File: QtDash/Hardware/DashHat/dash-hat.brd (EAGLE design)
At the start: 107.8 x 66.8 mm, 163 parts, among them IC1 LMV614, IC2 MCP3X083008, IC3 MCP23017SS, IC4 LM358D, IC5 IL300, IC6 TSV912D, IC7 IL300, IC8 TSV912D, IC9 DS1374, J1 CONN_20X2, J10 455-1750-1-ND, J11 455-1750-1-ND, J15 VSS_IN, J16 TACH_IN, J6 VOLVO_CONN_31, J7 VOLVO_CONN_32, J8 455-1750-1-ND, J9 455-1750-1-ND, Y1 ECX-.327-6-34RR

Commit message: bugfix/hardware-revA-issues: 	- moved alternator D+ supply to fuse 16 12V supply 	- added datasheet for new LED backlit screen 	- added mount stls
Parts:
- moved R82 42.7 mm to (105.2, 21.3), turned to 270 degrees
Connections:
- net 12V: no longer R82.2
- net 12V-FUSE_16: now also R82.2
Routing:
- net CHARGING_N: track 44.6 -> 30.9 mm
- net 12V-FUSE_16: track 0.00 -> 12.4 mm
- net OUT9: track 26.8 -> 29.1 mm
- net OUT10: track 24.7 -> 26.3 mm
- net GND: vias 36 -> 38
- added copper zone on layer 1, net 12V-FUSE_16
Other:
- board size 107.8 x 66.8 mm -> 110.9 x 66.8 mm
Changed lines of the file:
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@@
 <setting verticaltext="up"/>
 </settings>
-<grid distance="10" unitdist="mil" unit="mil" style="lines" multiple="1" display="yes" altdistance="1" altunitdist="mil" altunit="mil"/>
+<grid distance="5" unitdist="mil" unit="mil" style="lines" multiple="1" display="yes" altdistance="1" altunitdist="mil" altunit="mil"/>
 <layers>
 <layer number="1" name="Top" color="4" fill="1" visible="yes" active="yes"/>
@@
 <hole x="4.142" y="3.5" drill="2.75"/>
 <hole x="4.142" y="61.5" drill="2.75"/>
-<wire x1="107.95" y1="63.792" x2="107.95" y2="2.746" width="0.4064" layer="20"/>
-<wire x1="107.95" y1="2.746" x2="104.95" y2="0" width="0.4064" layer="20" curve="-90"/>
-<wire x1="104.95" y1="0" x2="3.142" y2="0" width="0.4064" layer="20"/>
+<wire x1="110.998" y1="63.792" x2="110.998" y2="2.746" width="0.4064" layer="20"/>
+<wire x1="110.998" y1="2.746" x2="107.998" y2="0" width="0.4064" layer="20" curve="-90"/>
+<wire x1="107.998" y1="0" x2="3.142" y2="0" width="0.4064" layer="20"/>
 <wire x1="3.142" y1="0" x2="0.142" y2="3" width="0.4064" layer="20" curve="-90"/>
 <wire x1="0.142" y1="3" x2="0.142" y2="65.062" width="0.4064" layer="20"/>
@@
 <wire x1="57.15" y1="64.516" x2="57.15" y2="66.08343125" width="0.4064" layer="20"/>
 <wire x1="57.15" y1="66.08343125" x2="57.86856875" y2="66.80185" width="0.4064" layer="20" curve="-90.011963"/>
-<wire x1="57.86856875" y1="66.80185" x2="104.696" y2="66.792" width="0.4064" layer="20"/>
-<wire x1="104.696" y1="66.792" x2="107.95" y2="63.792" width="0.4064" layer="20" curve="-90"/>
+<wire x1="57.86856875" y1="66.80185" x2="107.744" y2="66.792" width="0.4064" layer="20"/>
+<wire x1="107.744" y1="66.792" x2="110.998" y2="63.792" width="0.4064" layer="20" curve="-90"/>
 <text x="50.038" y="63.754" size="1.016" layer="25" font="vector" rot="R180">Volvo 240 Pi Dash Adapter
 Rev B. Jan 2022
@@
 <wire x1="7.8618" y1="25.233" x2="9.8618" y2="25.233" width="0.001" layer="57"/>
 <wire x1="7.8618" y1="21.433" x2="7.8618" y2="25.233" width="0.001" layer="57"/>
+<hole x="107.752" y="3.5" drill="2.75"/>
+<hole x="107.752" y="61.5" drill="2.75"/>
 </plain>
 <attributes>
@@
 <element name="R78" library="digital_dash" package="0603" value="1k" x="9.652" y="59.69" rot="R180"/>
 <element name="R79" library="digital_dash" package="0603" value="1k" x="14.732" y="59.69" rot="R180"/>
-<element name="R82" library="resistor" package="0617/17" value="" x="95.758" y="62.992" rot="R180"/>
+<element name="R82" library="resistor" package="0617/17" value="" x="105.156" y="21.336" rot="R270"/>
 </elements>
 <signals>
@@
 <wire x1="27.94" y1="53.086" x2="27.94" y2="53.848" width="0.3048" layer="1"/>
 <wire x1="27.92" y1="53.086" x2="27.94" y2="53.086" width="0.3048" layer="1"/>
+<via x="33.909" y="33.274" extent="1-16" drill="0.5"/>
+<via x="33.909" y="32.258" extent="1-16" drill="0.5"/>
 </signal>
 <signal name="5V">
@@
 <wire x1="80.838" y1="23.03" x2="80.754" y2="23.114" width="0.6096" layer="16"/>
 <wire x1="80.754" y1="23.114" x2="79.375" y2="23.114" width="0.6096" layer="16"/>
-<contactref element="R82" pad="2"/>
 <via x="77.47" y="63.754" extent="1-16" drill="0.5"/>
 <via x="80.01" y="65.024" extent="1-16" drill="0.5"/>
@@
 <wire x1="41.891" y1="31.935" x2="41.91" y2="31.916" width="0.3048" layer="1"/>
 <wire x1="41.91" y1="31.916" x2="41.91" y2="26.67" width="0.3048" layer="1"/>
-<wire x1="41.91" y1="26.67" x2="49.872" y2="18.708" width="0.3048" layer="1"/>
-<wire x1="49.872" y1="18.708" x2="55.118" y2="18.708" width="0.3048" layer="1"/>
 <wire x1="57.9755" y1="18.542" x2="57.8095" y2="18.708" width="0.3048" layer="1"/>
 <wire x1="57.8095" y1="18.708" x2="55.118" y2="18.708" width="0.3048" layer="1"/>
+<wire x1="41.91" y1="26.67" x2="43.434" y2="25.146" width="0.3048" layer="1"/>
+<wire x1="43.434" y1="25.146" x2="51.054" y2="25.146" width="0.3048" layer="1"/>
+<wire x1="51.054" y1="25.146" x2="51.562" y2="24.638" width="0.3048" layer="1"/>
+<wire x1="51.562" y1="24.638" x2="51.562" y2="21.844" width="0.3048" layer="1"/>
+<wire x1="51.562" y1="21.844" x2="54.698" y2="18.708" width="0.3048" layer="1"/>
+<wire x1="54.698" y1="18.708" x2="55.118" y2="18.708" width="0.3048" layer="1"/>
 </signal>
 <signal name="OUT9">
@@
 <wire x1="57.8095" y1="15.836" x2="55.118" y2="15.836" width="0.3048" layer="1"/>
 <wire x1="41.241" y1="31.935" x2="41.241" y2="26.323" width="0.3048" layer="1"/>
-<wire x1="41.241" y1="26.323" x2="51.728" y2="15.836" width="0.3048" layer="1"/>
-<wire x1="51.728" y1="15.836" x2="55.118" y2="15.836" width="0.3048" layer="1"/>
+<wire x1="41.241" y1="26.323" x2="43.18" y2="24.384" width="0.3048" layer="1"/>
+<wire x1="43.18" y1="24.384" x2="50.546" y2="24.384" width="0.3048" layer="1"/>
+<wire x1="50.546" y1="24.384" x2="50.8" y2="24.13" width="0.3048" layer="1"/>
+<wire x1="50.8" y1="24.13" x2="50.8" y2="21.59" width="0.3048" layer="1"/>
+<wire x1="50.8" y1="21.59" x2="53.848" y2="18.542" width="0.3048" layer="1"/>
+<wire x1="53.848" y1="18.542" x2="53.848" y2="17.018" width="0.3048" layer="1"/>
+<wire x1="53.848" y1="17.018" x2="55.03" y2="15.836" width="0.3048" layer="1"/>
+<wire x1="55.03" y1="15.836" x2="55.118" y2="15.836" width="0.3048" layer="1"/>
 </signal>
 <signal name="IN11P">
@@
 <polygon width="0.3048" layer="1" isolate="0.3048" orphans="yes" thermals="no" rank="2">
 <vertex x="66.04" y="66.802"/>
-<vertex x="106.394240625" y="66.802"/>
-<vertex x="108.1902375" y="64.99223125"/>
-<vertex x="107.70684375" y="1.425953125"/>
+<vertex x="109.188240625" y="66.802"/>
+<vertex x="110.9842375" y="64.99223125"/>
+<vertex x="110.50084375" y="0.917953125"/>
 <vertex x="106.27004375" y="0"/>
 <vertex x="66.04" y="0"/>
@@
 <contactref element="C13" pad="2"/>
 <polygon width="0.3048" layer="16" isolate="0.3048" orphans="yes" thermals="no">
-<vertex x="108.196428125" y="64.810596875"/>
-<vertex x="107.956803125" y="1.789221875"/>
+<vertex x="111.244428125" y="65.064596875"/>
+<vertex x="110.750803125" y="1.281221875"/>
 <vertex x="106.160765625" y="0"/>
 <vertex x="66.04" y="0"/>
 <vertex x="66.04" y="66.802"/>
-<vertex x="106.212640625" y="66.802"/>
+<vertex x="109.514640625" y="66.802"/>
 </polygon>
 <via x="73.914" y="17.526" extent="1-16" drill="0.5"/>
@@
 <polygon width="0.3048" layer="15" isolate="0.3048">
 <vertex x="66.04" y="66.548"/>
-<vertex x="107.95" y="66.548"/>
-<vertex x="107.95" y="0"/>
+<vertex x="110.744" y="66.294"/>
+<vertex x="110.744" y="-0.254"/>
 <vertex x="66.04" y="0"/>
 </polygon>
@@
 <wire x1="89.662" y1="59.69" x2="105.918" y2="59.69" width="0.6096" layer="16"/>
 <wire x1="105.918" y1="59.69" x2="106.934" y2="58.674" width="0.6096" layer="16"/>
-<wire x1="106.934" y1="58.674" x2="106.934" y2="20.719609375" width="0.6096" layer="16"/>
-<wire x1="106.934" y1="20.719609375" x2="90.024390625" y2="3.81" width="0.6096" layer="16"/>
-<wire x1="90.024390625" y1="3.81" x2="57.658" y2="3.81" width="0.6096" layer="16"/>
+<wire x1="90.043" y1="3.81" x2="57.658" y2="3.81" width="0.6096" layer="16"/>
 <wire x1="57.658" y1="3.81" x2="54.864" y2="6.858" width="0.6096" layer="16"/>
 <wire x1="54.864" y1="6.858" x2="51.816" y2="6.858" width="0.6096" layer="16"/>
@@
 <wire x1="10.414" y1="5.842" x2="10.922" y2="6.35" width="0.6096" layer="1"/>
 <wire x1="10.922" y1="6.35" x2="12.3952" y2="6.35" width="0.6096" layer="1"/>
+<wire x1="106.934" y1="58.674" x2="106.934" y2="38.735" width="0.6096" layer="16"/>
+<wire x1="106.934" y1="38.735" x2="102.489" y2="34.29" width="0.6096" layer="16"/>
+<wire x1="102.489" y1="34.29" x2="102.489" y2="16.256" width="0.6096" layer="16"/>
+<wire x1="102.489" y1="16.256" x2="90.043" y2="3.81" width="0.6096" layer="16"/>
 </signal>
 <signal name="HIGH_BEAM_P">
@@
 <wire x1="96.012" y1="52.07" x2="97.616" y2="50.466" width="0.6096" layer="16"/>
 <wire x1="97.616" y1="50.466" x2="101.878" y2="50.466" width="0.6096" layer="16"/>
-<wire x1="101.878" y1="50.466" x2="104.654" y2="53.242" width="1.27" layer="1"/>
 <contactref element="R82" pad="1"/>
-<wire x1="104.654" y1="53.242" x2="104.648" y2="53.756" width="1.27" layer="1"/>
-<wire x1="104.648" y1="53.756" x2="104.648" y2="62.992" width="1.27" layer="1"/>
 <polygon width="0.4064" layer="1" isolate="0.3048" orphans="yes" thermals="no">
-<vertex x="107.95" y="53.848"/>
-<vertex x="107.95" y="63.28958125"/>
-<vertex x="107.23158125" y="64.008"/>
-<vertex x="102.82641875" y="64.008"/>
-<vertex x="102.108" y="63.28958125"/>
-<vertex x="102.108" y="53.848"/>
-<vertex x="99.568" y="51.308"/>
-<vertex x="99.568" y="49.53"/>
-<vertex x="100.838" y="48.26"/>
-<vertex x="102.362" y="48.26"/>
+<vertex x="103.378" y="28.956"/>
+<vertex x="110.49" y="28.99958125"/>
+<vertex x="110.53358125" y="51.308"/>
+<vertex x="109.20181875" y="52.5272"/>
+<vertex x="104.3432" y="52.54538125"/>
+<vertex x="101.092" y="52.578"/>
+<vertex x="99.822" y="51.308"/>
+<vertex x="99.822" y="49.429809375"/>
+<vertex x="100.737809375" y="48.514"/>
+<vertex x="102.810040625" y="48.514"/>
+<vertex x="103.378" y="47.946040625"/>
 </polygon>
 </signal>
@@
 <signal name="12V-FUSE_16">
 <contactref element="J7" pad="A"/>
+<contactref element="R82" pad="2"/>
+<wire x1="96.913046875" y1="17.978403125" x2="102.925596875" y2="17.978403125" width="1.27" layer="1"/>
+<wire x1="102.925596875" y1="17.978403125" x2="105.156" y2="15.621" width="1.27" layer="1"/>
+<wire x1="105.156" y1="15.621" x2="105.156" y2="12.446" width="1.27" layer="1"/>
+<polygon width="0.3048" layer="1" isolate="0.3048" thermals="no">
+<vertex x="94.742" y="19.812"/>
+<vertex x="94.742" y="16.764"/>
+<vertex x="100.33" y="11.176"/>
+<vertex x="105.918" y="11.176"/>
+<vertex x="106.172" y="11.43"/>
+<vertex x="106.172" y="19.558"/>
+<vertex x="105.664" y="20.066"/>
+<vertex x="94.996" y="20.066"/>
+</polygon>
 </signal>
 <signal name="OD_LAMP_AUTO_P">

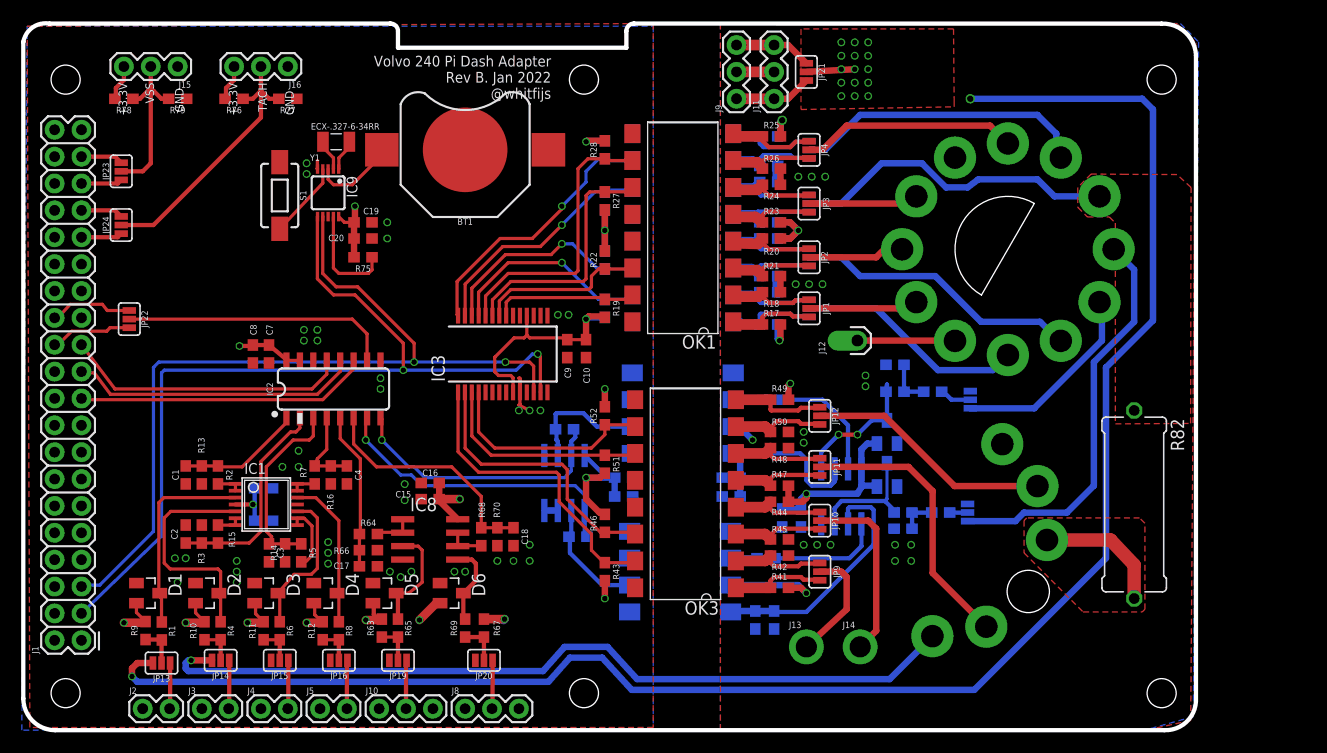
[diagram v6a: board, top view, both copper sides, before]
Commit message: bugfix/hardware-revA-issues: 	- adjusted mounts to be inset about a mm 	- added mounts to align the screen upside down
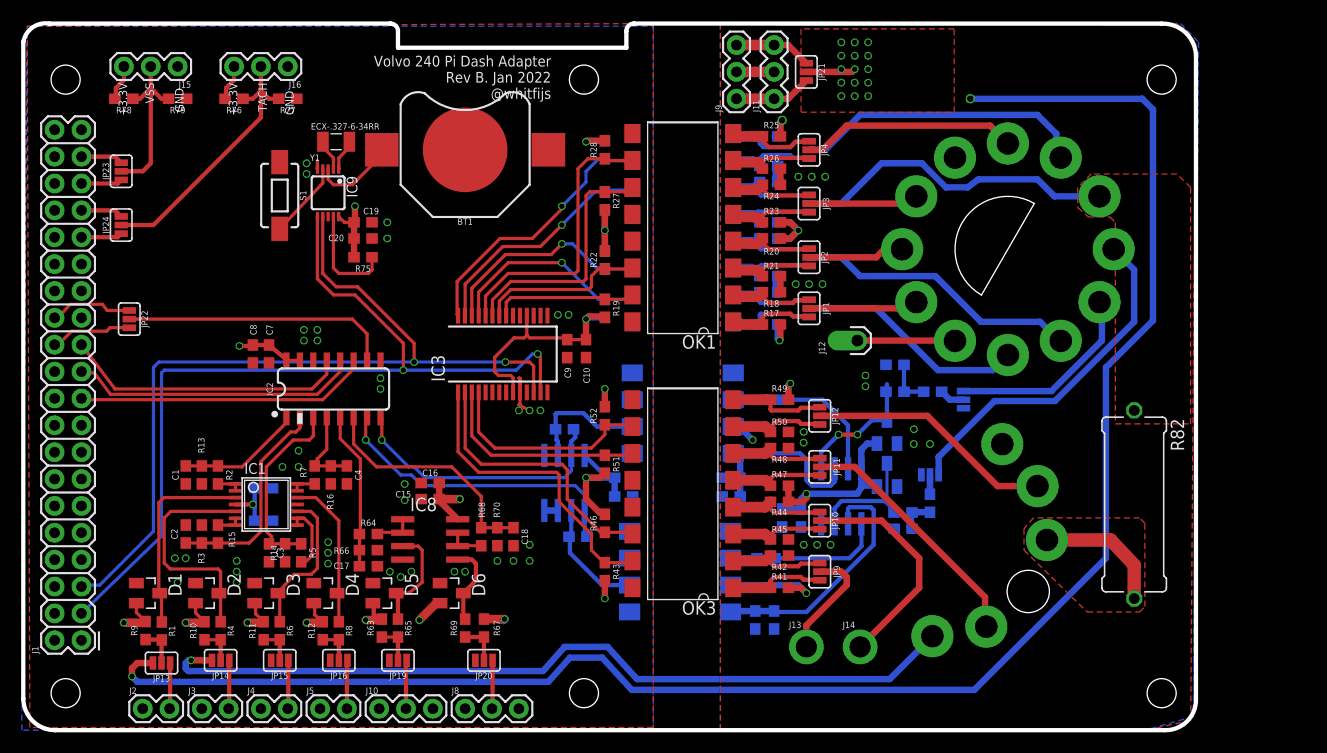
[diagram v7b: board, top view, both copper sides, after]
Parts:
- moved JP17 5.03 mm to (85.9, 24.1), turned to 180 degrees
- moved R73 1.35 mm to (85.9, 21.5), turned to 270 degrees
- moved JP18 0.64 mm to (89.0, 31.2), turned to 90 degrees
- moved OK3 0.25 mm to (62.5, 22.4)
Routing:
- net DIMMER_VOUT: track 38.1 -> 33.1 mm
- net CHECK_ENGINE_N: track 17.5 -> 21.6 mm
- net PARKING_BRAKE_N: track 26.5 -> 23.6 mm
- net N$19: track 3.26 -> 2.55 mm
- net GND-ISO: vias 17 -> 16
- added copper zone on layer 2, net GND-ISO

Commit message: bugfix/hardware-revA-issues: 	- added outputs solder points for fuse 16 and fuse 8 power 	- added 12V input solder points switched power? 	- added some ground vias on for 5V ground return path -- things were a little tight 	- extended board to add output power solder points
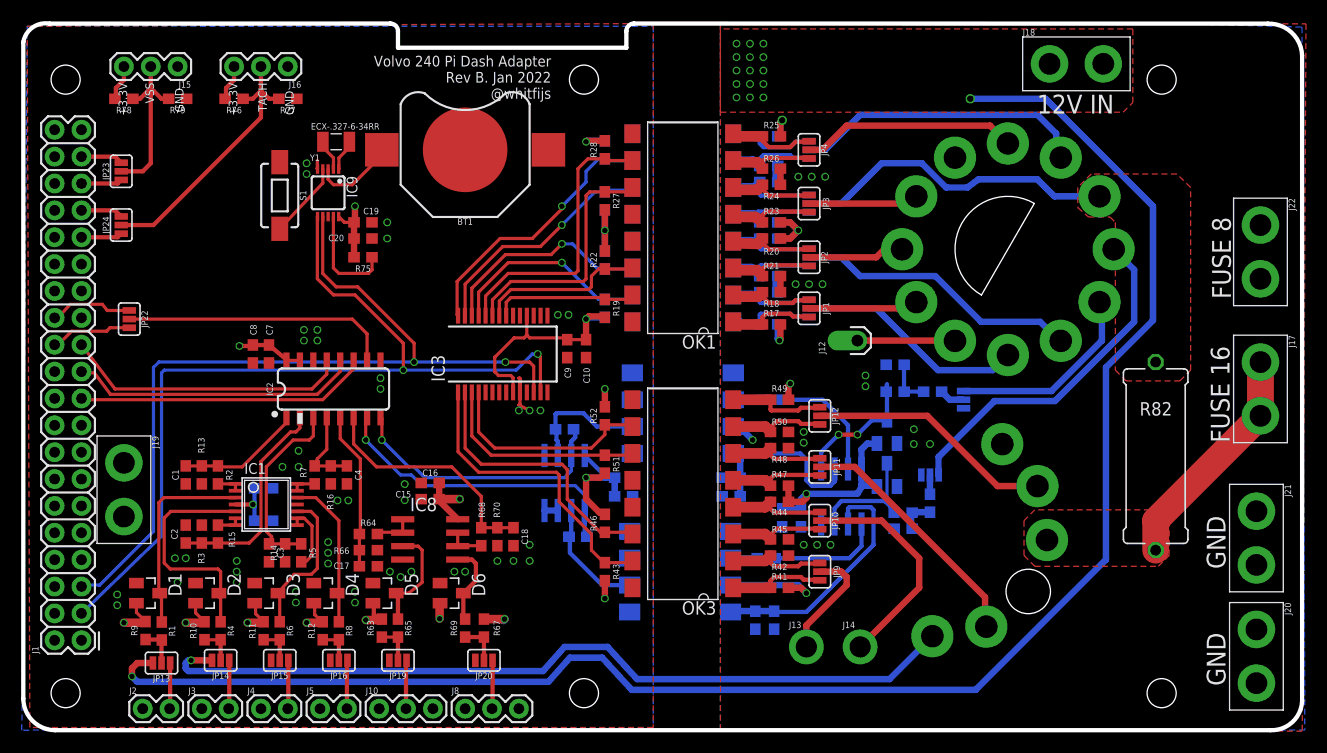
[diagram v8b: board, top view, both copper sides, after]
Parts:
- removed J11, J9: 455-1750-1-ND, SparkFun-Connectors:1X03
- removed JP21: JUMPER-SMT_3_NO_SILK, SparkFun-Jumpers:SMT-JUMPER_3_NO_SILK
- added J17, J18, J19, J20, J21, J22: (no value), SparkFun-Connectors:1X02_XTRA_BIG
- moved R82 5.00 mm to (107.2, 25.9)
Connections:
- removed net N$10: J11.1, J9.1, JP21.3
- removed net N$12: J11.2, J9.2
- removed net N$14: J11.3, J9.3, JP21.1
- net 12V: now also J18.1, J18.2; no longer JP21.2
- net 12V-FUSE_16: now also J17.1, J17.2
- net 12V-FUSE_8: now also J22.1, J22.2
- net 5V: now also J19.2
- net GND: now also J19.1
- net GND-ISO: now also J20.1, J20.2, J21.1, J21.2
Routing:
- net 12V-FUSE_16: track 12.4 -> 21.9 mm
- net N$10: track 7.32 -> 0.00 mm
- net N$14: track 7.32 -> 0.00 mm
- net COOLANT_TEMP_SENSOR: track 171.0 -> 165.7 mm
- net 12V-FUSE_8: track 18.8 -> 23.9 mm
- net 12V: track 52.6 -> 48.0 mm
- net N$12: track 3.56 -> 0.00 mm
- net 5V: track 34.7 -> 33.6 mm
- net GND: vias 38 -> 46
- added copper zone on layer 2, net 12V-FUSE_8
- added copper zone on layer 2, net GND
- added copper zone on layer 15, net N$42
- removed copper zone on layer 2, net N$40
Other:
- board size 110.9 x 66.8 mm -> 120.9 x 66.8 mm
- board text added: "12V IN"
- board text added: "FUSE 16"
- board text added: "FUSE 8"
